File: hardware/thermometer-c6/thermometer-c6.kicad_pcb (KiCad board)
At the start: 2 copper layers, 48 x 35 mm, 101 parts, among them J1 JST-PH-2 BAT, J2 MEAS_HDR, J3 USB-C, J4 EPD FPC24 0.5mm, J5 DEBUG, Q1 AO3401A, Q2 AO3401A, Q3 Si1308EDL, Q4 AO3401A, Q5 2N7002, Q6 AO3401A, SW1 RESET, SW2 BOOT, U1 ESP32-C6-MINI-1-N4, U2 RT9080-33GJ5, U3 USBLC6-2SC6, U4 MCP73831-2, U5 BMP581, U6 BMP585, Y1 32.768kHz FC-135

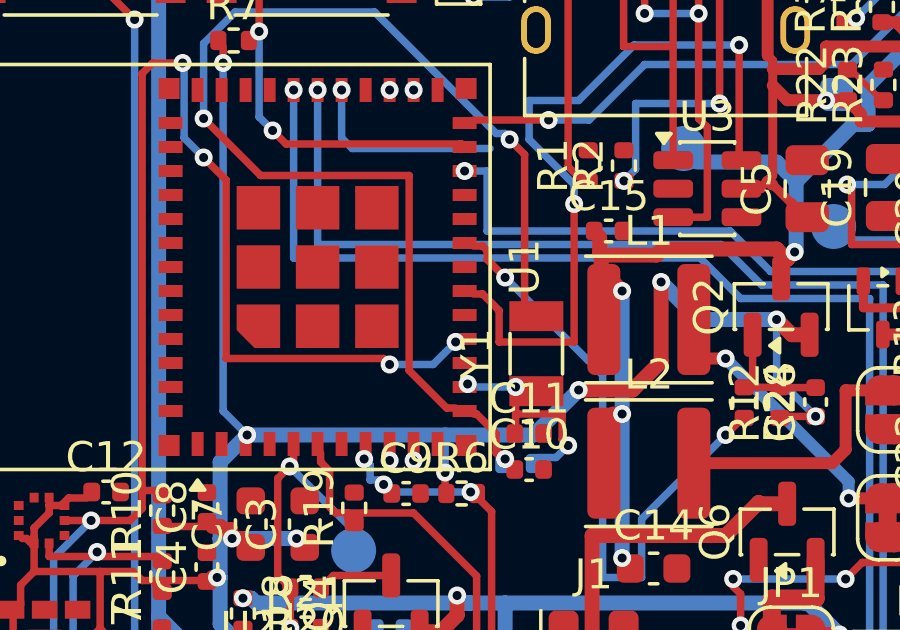
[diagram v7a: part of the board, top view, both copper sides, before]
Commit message: Anchor SCL's U1.16 escape via beside the pad
The stub joins the east pad row's via strip; SCL's remaining straggler
is now the west-column crossing to this island, not the pad escape.

Co-Authored-By: Claude Fable 5 <noreply@anthropic.com>
Claude-Session: https://claude.ai/code/session_01SwxdfLoUnFYH7rYYztLkHV
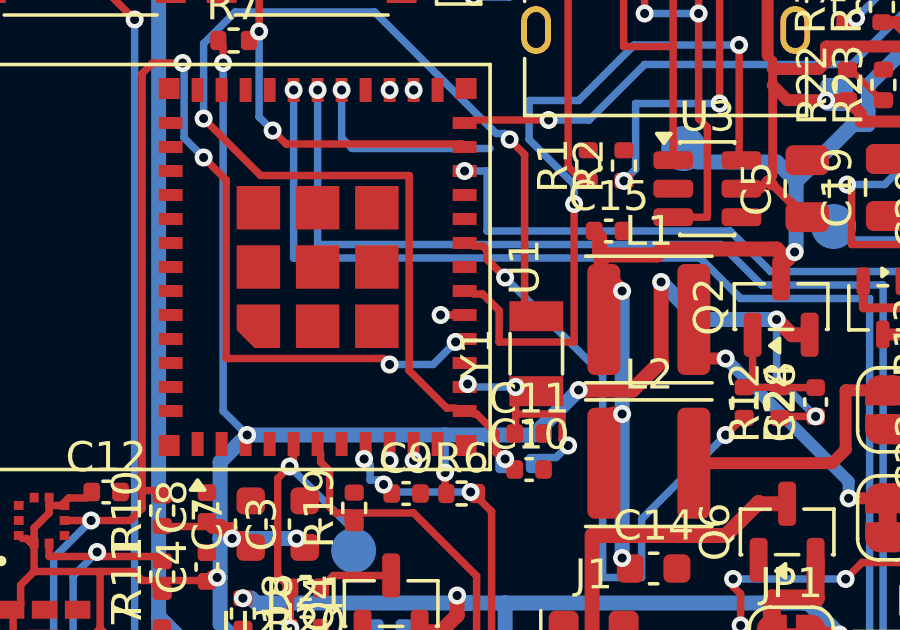
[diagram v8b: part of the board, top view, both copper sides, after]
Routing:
- net SCL: track 13.5 -> 14.3 mm, vias 2 -> 3
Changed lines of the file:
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@@
 	)
 	(segment
+		(start 116.25 115.55)
+		(end 115.9 115.55)
+		(width 0.25)
+		(layer "F.Cu")
+		(net "SCL")
+	)
+	(segment
 		(start 116.4 103.4)
 		(end 115.5 102.5)
@@
 	)
 	(segment
+		(start 116.7 115.55)
+		(end 116.25 115.55)
+		(width 0.25)
+		(layer "F.Cu")
+		(net "SCL")
+	)
+	(segment
 		(start 116.8 102.6)
 		(end 117.15 102.25)
@@
 	)
 	(via
+		(at 115.9 115.55)
+		(size 0.6)
+		(drill 0.3)
+		(layers "F.Cu" "B.Cu")
+		(net "SCL")
+	)
+	(via
